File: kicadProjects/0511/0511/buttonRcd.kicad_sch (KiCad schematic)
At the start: 4 parts, among them SW1 SW_Push

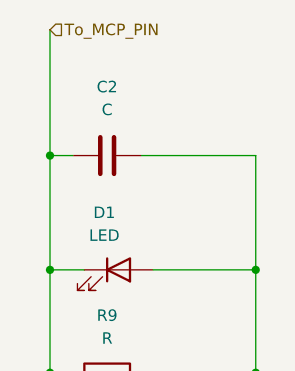
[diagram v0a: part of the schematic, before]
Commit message: ajout 2 mcp23017
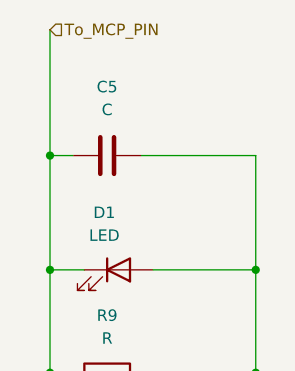
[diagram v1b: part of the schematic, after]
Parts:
- C5: renamed from C2; footprint (none) -> Capacitor_THT:CP_Axial_L10.0mm_D4.5mm_P15.00mm_Horizontal
- D1: footprint (none) -> Diode_THT:D_DO-41_SOD81_P10.16mm_Horizontal
- R9: footprint (none) -> Resistor_SMD:R_0603_1608Metric
- SW1: footprint (none) -> Button_Switch_Keyboard:SW_Cherry_MX_1.00u_PCB

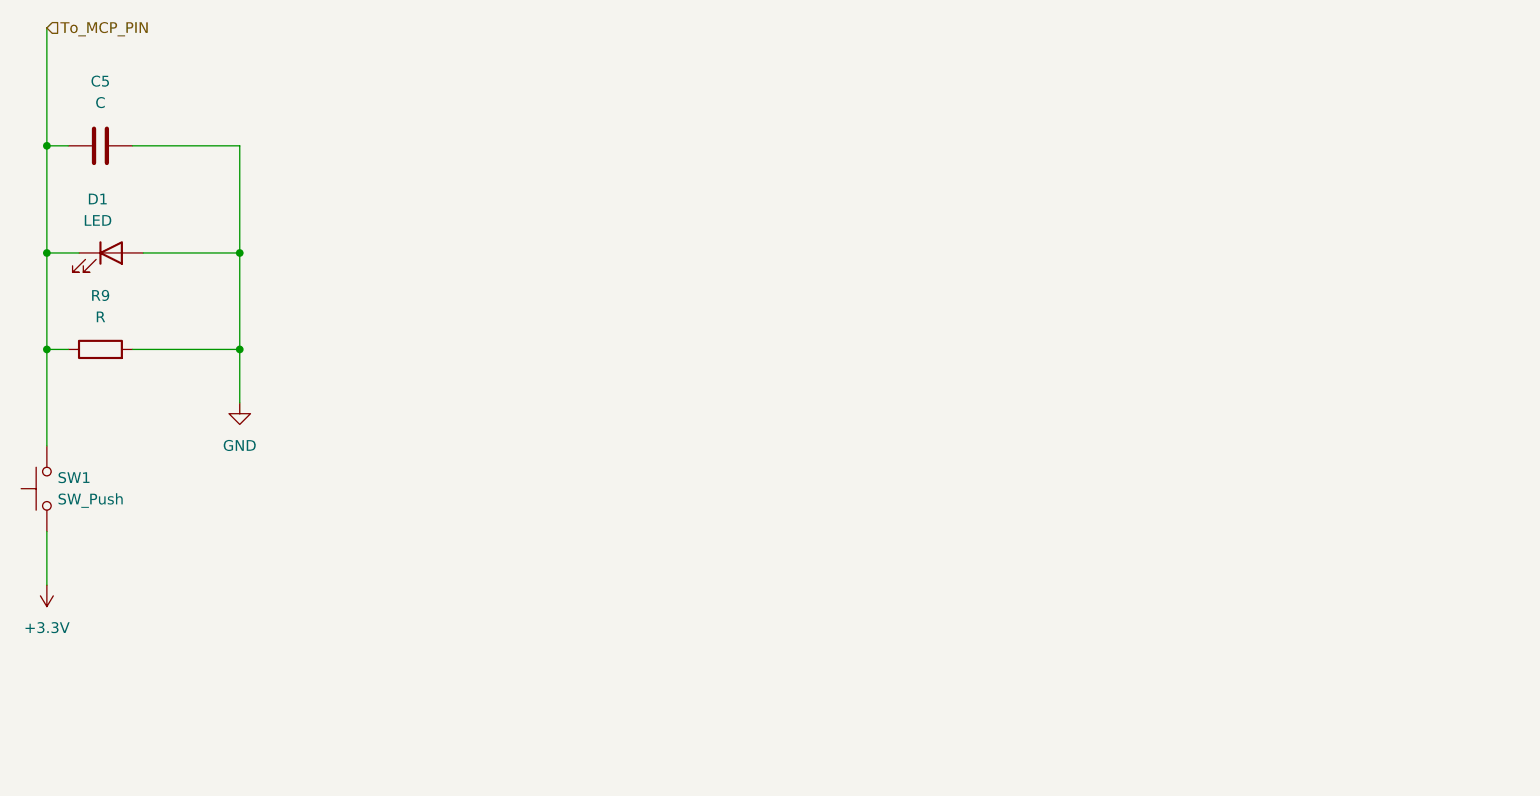
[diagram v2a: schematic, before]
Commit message: adaptation empreintes mcp23017 ajout valeurs aux résistances corrections empreintes des résistances et condensateurs
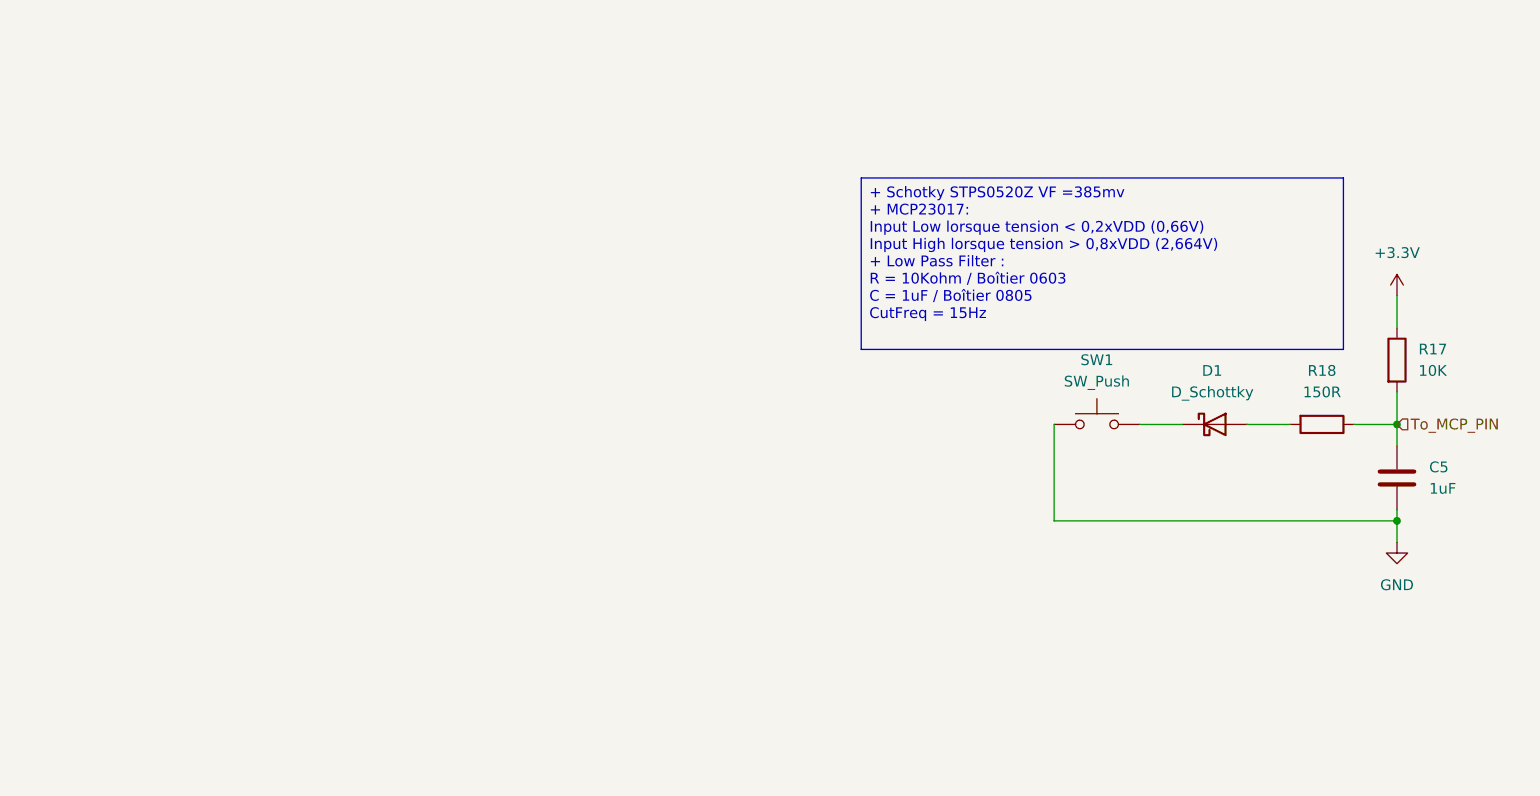
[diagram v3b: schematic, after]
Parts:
- removed D1: LED, Diode_THT:D_DO-41_SOD81_P10.16mm_Horizontal, symbol Device:LED
- removed R9: R, Resistor_SMD:R_0603_1608Metric, symbol Device:R
- added D1: D_Schottky, Diode_SMD:D_SOD-123, symbol Device:D_Schottky
- added R17: 10K, Resistor_SMD:R_0603_1608Metric, symbol Device:R
- added R18: 150R, Resistor_SMD:R_0603_1608Metric, symbol Device:R
- C5: value C -> 1uF; footprint Capacitor_THT:CP_Axial_L10.0mm_D4.5mm_P15.00mm_Horizontal -> Capacitor_SMD:C_0603_1608Metric
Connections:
- net +3.3V: now also R17.1; no longer SW1.1
- net GND: now also SW1.1
- net To_MCP_PIN: now also R17.2, R18.1; no longer SW1.2
- new net: D1.1 (K), SW1.2
- new net: D1.2 (A), R18.2

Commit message: assignation empreintes
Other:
- moved on the sheet: C5, D1, R17, R18, SW1

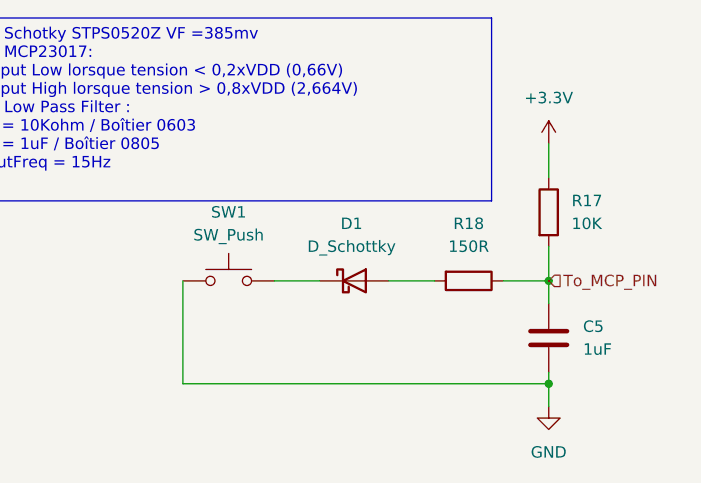
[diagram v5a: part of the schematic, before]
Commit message: started to annotate and place buttons on pcb
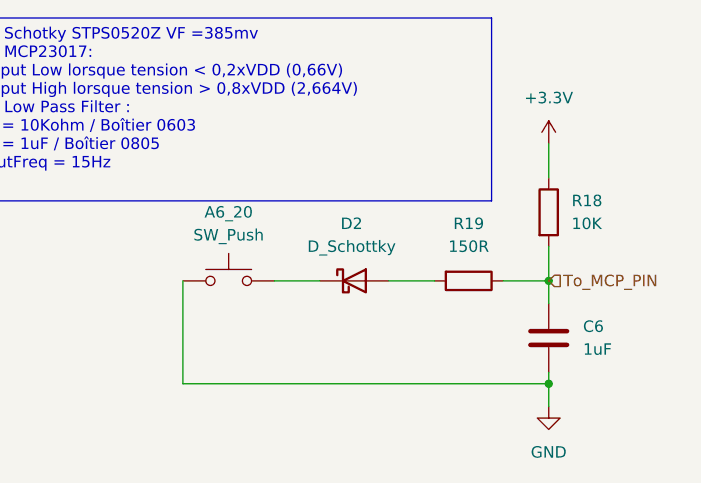
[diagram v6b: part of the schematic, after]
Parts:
- renumbered SW1 to A6_20, C5 to C6, D1 to D2, R17 to R18, R18 to R19

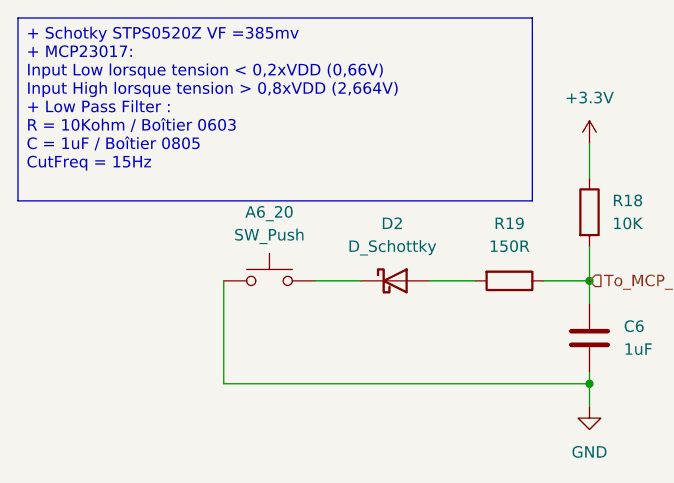
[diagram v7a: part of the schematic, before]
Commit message: poursuite placement et nommage références
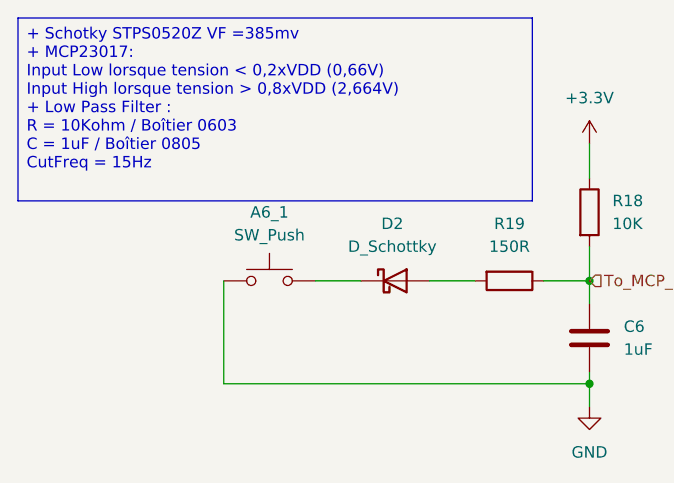
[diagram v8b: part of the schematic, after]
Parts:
- renumbered A6_20 to A6_1
